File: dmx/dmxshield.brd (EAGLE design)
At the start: 100 x 80 mm, 17 parts, among them IC1 MAX3468CPA, X1 NC5FAV

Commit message: use on board IC
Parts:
- removed SV1: (no value), con-dil:IC16P
- added SV2: (no value), con-lstb:MA04-2
- IC1: value MAX3468CPA -> MAX3468CSA; device maxim:DIL08 -> maxim:SO08
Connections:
- removed net N$12: C1.1, DC1.14, IC1.8, OK1.2, OK2.8, OK3.8, R8.1, R9.1
- removed net N$17: C1.2, DC1.15, OK2.5, OK3.5, R1.1, X1.1, X1.G
- removed net N$7: R5.1, SV1.11
- new net N$3: R5.1, SV2.5
- new net VCC: C1.1, DC1.14, DC1.24, IC1.8, OK1.2, OK2.8, OK3.8, R8.1, R9.1, SV2.4
- net GND: now also C1.2, DC1.13, DC1.15, OK1.5, OK2.5, OK3.5, R1.1, SV2.8, X1.1, X1.G
- net N$1: now also SV2.7; no longer SV1.9
- net N$16: now also R6.1, SV2.3; no longer DC1.13, OK1.5, SV1.1
- net N$5: no longer DC1.24, SV1.4
- net N$6: now also LED1.A; no longer R6.1, SV1.10
- net N$8: no longer LED1.A

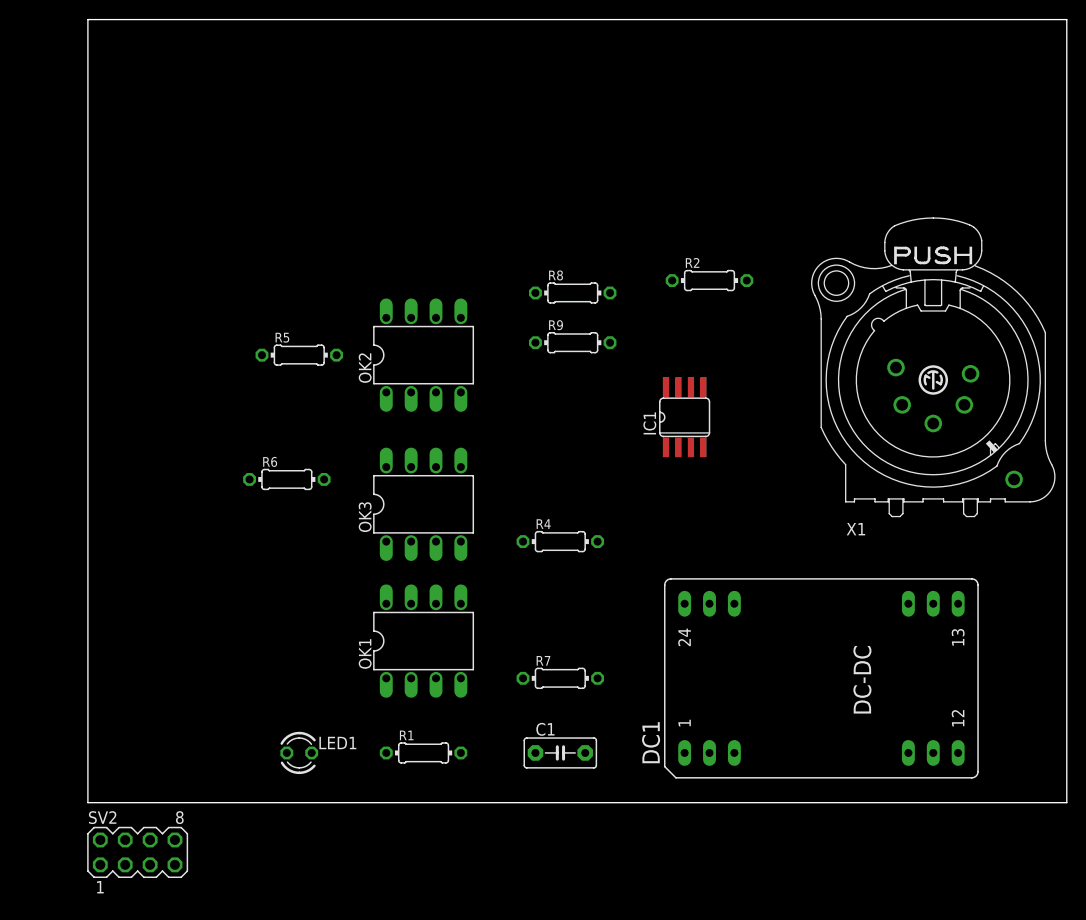
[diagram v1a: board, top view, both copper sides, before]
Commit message: change all components to surface mounted
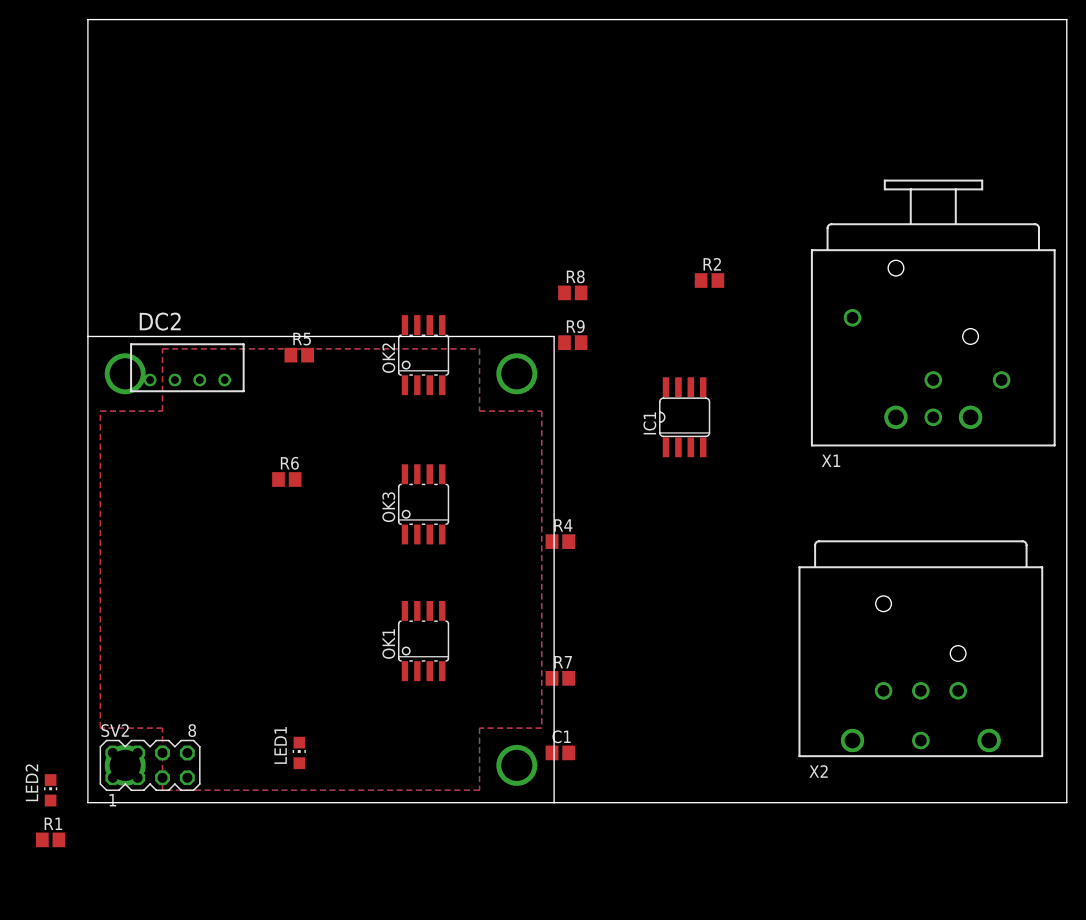
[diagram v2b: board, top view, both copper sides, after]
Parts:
- removed DC1: (no value), dc-dc-converter:DCW
- added DC2: VA-2424S1.5, dc-dc-converter:4SIL
- added LED2: (no value), led:CHIP-LED0805
- added X2: NC5MBN-B, con-neutrik_ag:NC5MBH-B
- C1: device capacitor-wima:C5B3 -> resistor:C0805
- LED1: device led:LED3MM -> led:CHIP-LED0805
- OK1, OK2, OK3: value 6N137 -> HCPL0600; device optocoupler:DIL08 -> optocoupler:SOIC08
- R1, R2, R4, R5, R6, R7, R8, R9: device resistor:0204/7 -> resistor:R0805
- X1: value NC5FAV -> NC5FBH-B; device con-neutrik_ag:NC5FAV -> con-neutrik_ag:NC5FBH-B
- moved R1 39.1 mm to (-3.81, -3.81)
- moved SV2 8.98 mm to (6.35, 3.81)
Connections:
- new net N$7: C1.2, DC2.3, IC1.5, LED2.C, OK2.5, OK3.5, OK3.7, X1.1, X1.G, X2.1, X2.G
- net GND: now also DC2.1; no longer C1.2, DC1.13, DC1.15, IC1.5, OK2.5, OK3.5, R1.1, X1.1, X1.G
- net N$11: now also LED2.A; no longer LED1.K
- net N$13: now also R1.1
- net N$14: now also X2.2
- net N$15: now also X2.3
- net N$5: now also LED1.A, OK1.3; no longer OK1.8, OK2.2, OK3.2, R4.2
- net N$6: now also C1.1, DC2.4, IC1.8, OK1.2, OK2.8, OK3.8, R8.1, R9.1; no longer LED1.A
- net N$9: now also LED1.C; no longer OK1.3
- net VCC: now also DC2.2, OK1.8, OK2.2, OK3.2, R4.2; no longer C1.1, DC1.14, DC1.24, IC1.8, OK1.2, OK2.8, OK3.8, R8.1, R9.1
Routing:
- added copper zone on layer 16, net N$17
- added copper zone on layer 1, net N$18
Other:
- outline, holes or cut-outs redrawn
- board text added: "(C) 2012, Demand Peripherals, Inc."
- board text added: "1"
- board text added: "10"
- board text added: "11"
- board text added: "12"
- board text added: "13"
- board text added: "14"
- board text added: "15"
- board text added: "16"
- board text added: "2"
- board text added: "3"
- board text added: "3.3V"
- board text added: "4"
- board text added: "5"
- board text added: "5.0V"
- board text added: "6"
- board text added: "7"
- board text added: "8"
- board text added: "9"
- board text added: "BB4"
- board text added: "C1"
- board text added: "C2"
- board text added: "C3"
- board text added: "C4"
- board text added: "Gnd"
- board text added: "IC1"
- board text added: "IC2"
- board text added: "IC3"
- board text added: "IC4"
- board text added: "PROTO, Rev A"
- board text added: "R1"
- board text added: "R2"
- board text added: "R3"
- board text added: "R4"
- board text added: "V2"
- board text added: "V3"
